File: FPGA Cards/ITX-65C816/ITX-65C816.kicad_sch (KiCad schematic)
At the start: 4 parts, among them J1 Conn_02x22_Odd_Even, U1 W65C816S6TQG-14

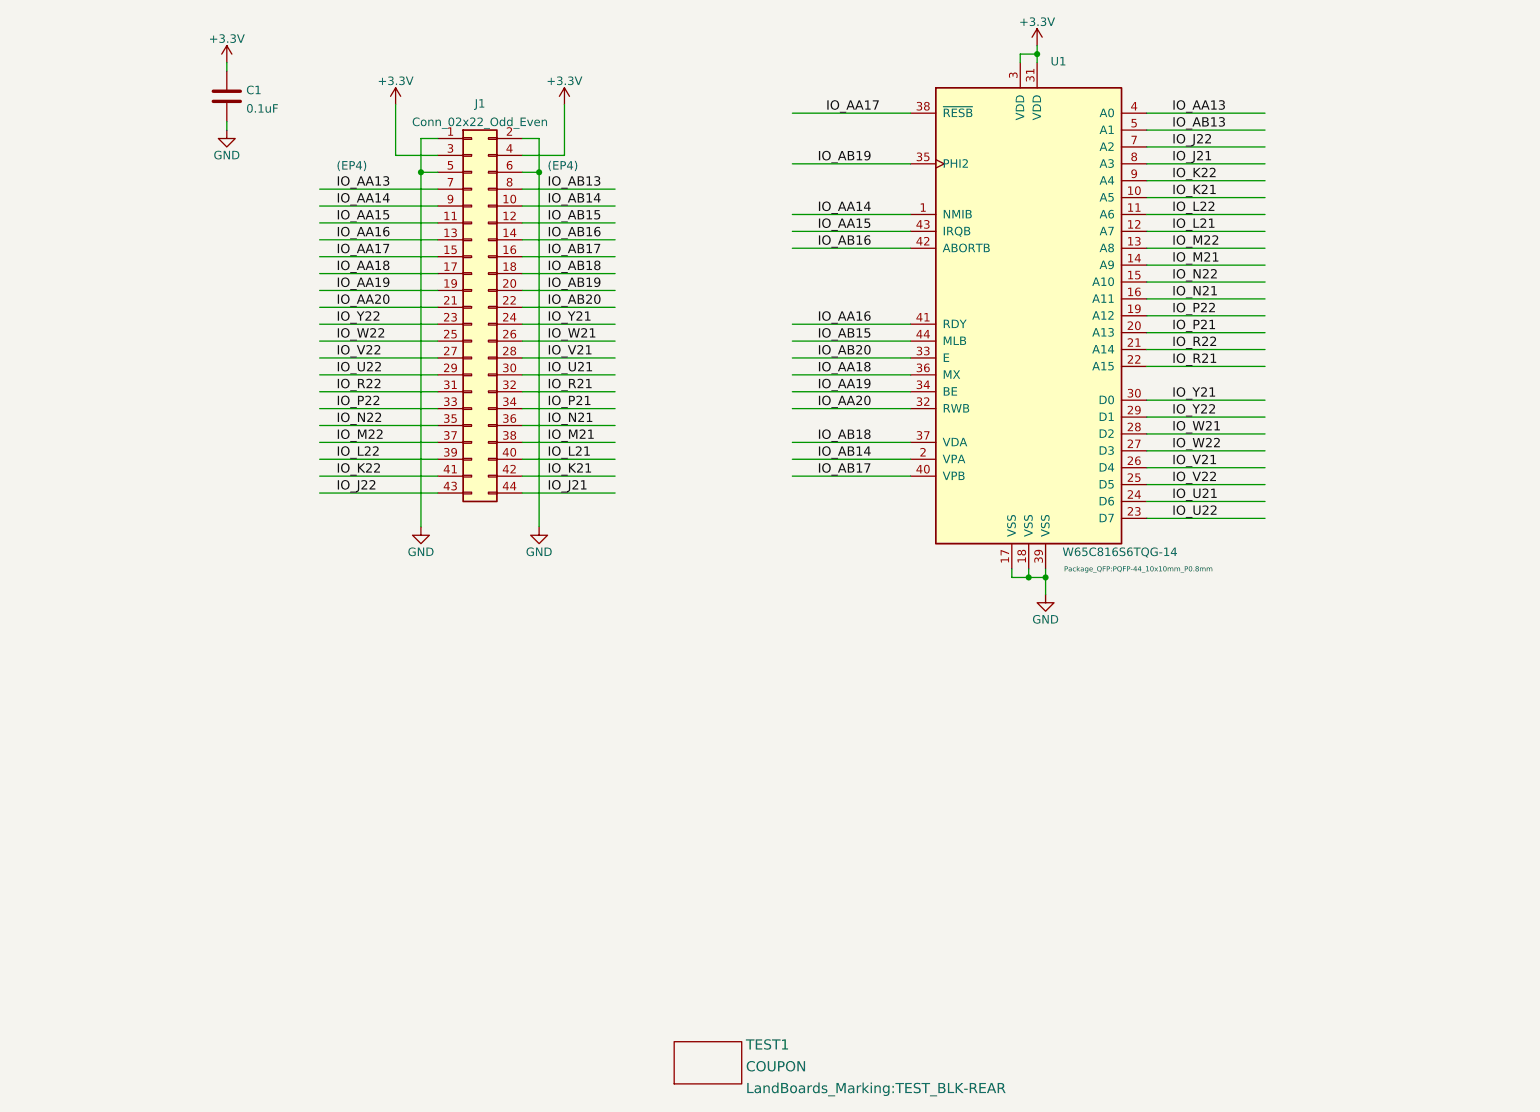
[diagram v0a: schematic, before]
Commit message: update ITX design files
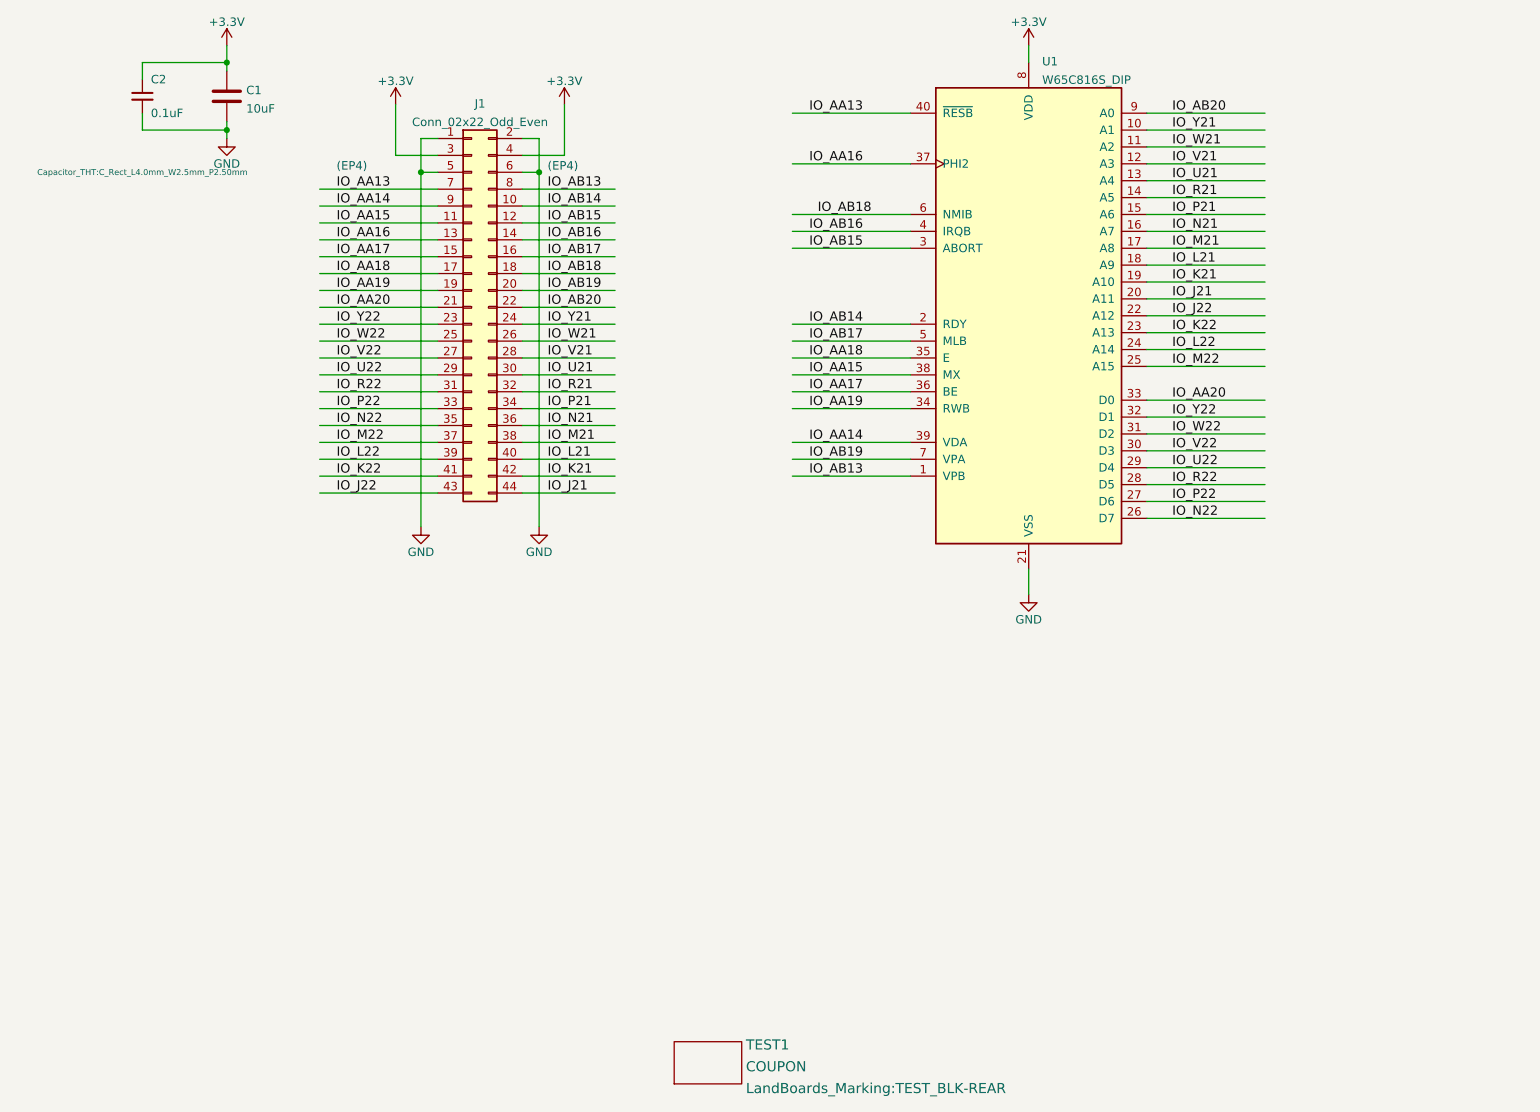
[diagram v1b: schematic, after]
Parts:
- removed U1: W65C816S6TQG-14, Package_QFP:PQFP-44_10x10mm_P0.8mm, symbol LandBoards_Semis:W65C816S
- added C2: 0.1uF, Capacitor_THT:C_Rect_L4.0mm_W2.5mm_P2.50mm, symbol Device:C_Small
- added U1: W65C816S_DIP, Package_DIP:DIP-40_W15.24mm_Socket, symbol LandBoards_Semis:W65C816S_DIP
- C1: value 0.1uF -> 10uF; footprint (none) -> Capacitor_THT:CP_Radial_D5.0mm_P2.50mm
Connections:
- net +3V3: now also C2.1, U1.8 (VDD)
- net GND: now also C2.2, U1.21 (VSS)
- net IO_AA13: now also U1.40 (~{RESB})
- net IO_AA14: now also U1.39 (VDA)
- net IO_AA15: now also U1.38 (MX)
- net IO_AA16: now also U1.37 (PHI2)
- net IO_AA17: now also U1.36 (BE)
- net IO_AA18: now also U1.35 (E)
- net IO_AA19: now also U1.34 (RWB)
- net IO_AA20: now also U1.33 (D0)
- net IO_AB13: now also U1.1 (VPB)
- net IO_AB14: now also U1.2 (RDY)
- net IO_AB15: now also U1.3 (ABORT)
- net IO_AB16: now also U1.4 (IRQB)
- net IO_AB17: now also U1.5 (MLB)
- net IO_AB18: now also U1.6 (NMIB)
- net IO_AB19: now also U1.7 (VPA)
- net IO_AB20: now also U1.9 (A0)
- net IO_J21: now also U1.20 (A11)
- net IO_J22: now also U1.22 (A12)
- net IO_K21: now also U1.19 (A10)
- net IO_K22: now also U1.23 (A13)
- net IO_L21: now also U1.18 (A9)
- net IO_L22: now also U1.24 (A14)
- net IO_M21: now also U1.17 (A8)
- net IO_M22: now also U1.25 (A15)
- net IO_N21: now also U1.16 (A7)
- net IO_N22: now also U1.26 (D7)
- net IO_P21: now also U1.15 (A6)
- net IO_P22: now also U1.27 (D6)
- net IO_R21: now also U1.14 (A5)
- net IO_R22: now also U1.28 (D5)
- net IO_U21: now also U1.13 (A4)
- net IO_U22: now also U1.29 (D4)
- net IO_V21: now also U1.12 (A3)
- net IO_V22: now also U1.30 (D3)
- net IO_W21: now also U1.11 (A2)
- net IO_W22: now also U1.31 (D2)
- net IO_Y21: now also U1.10 (A1)
- net IO_Y22: now also U1.32 (D1)

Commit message: ITX cards
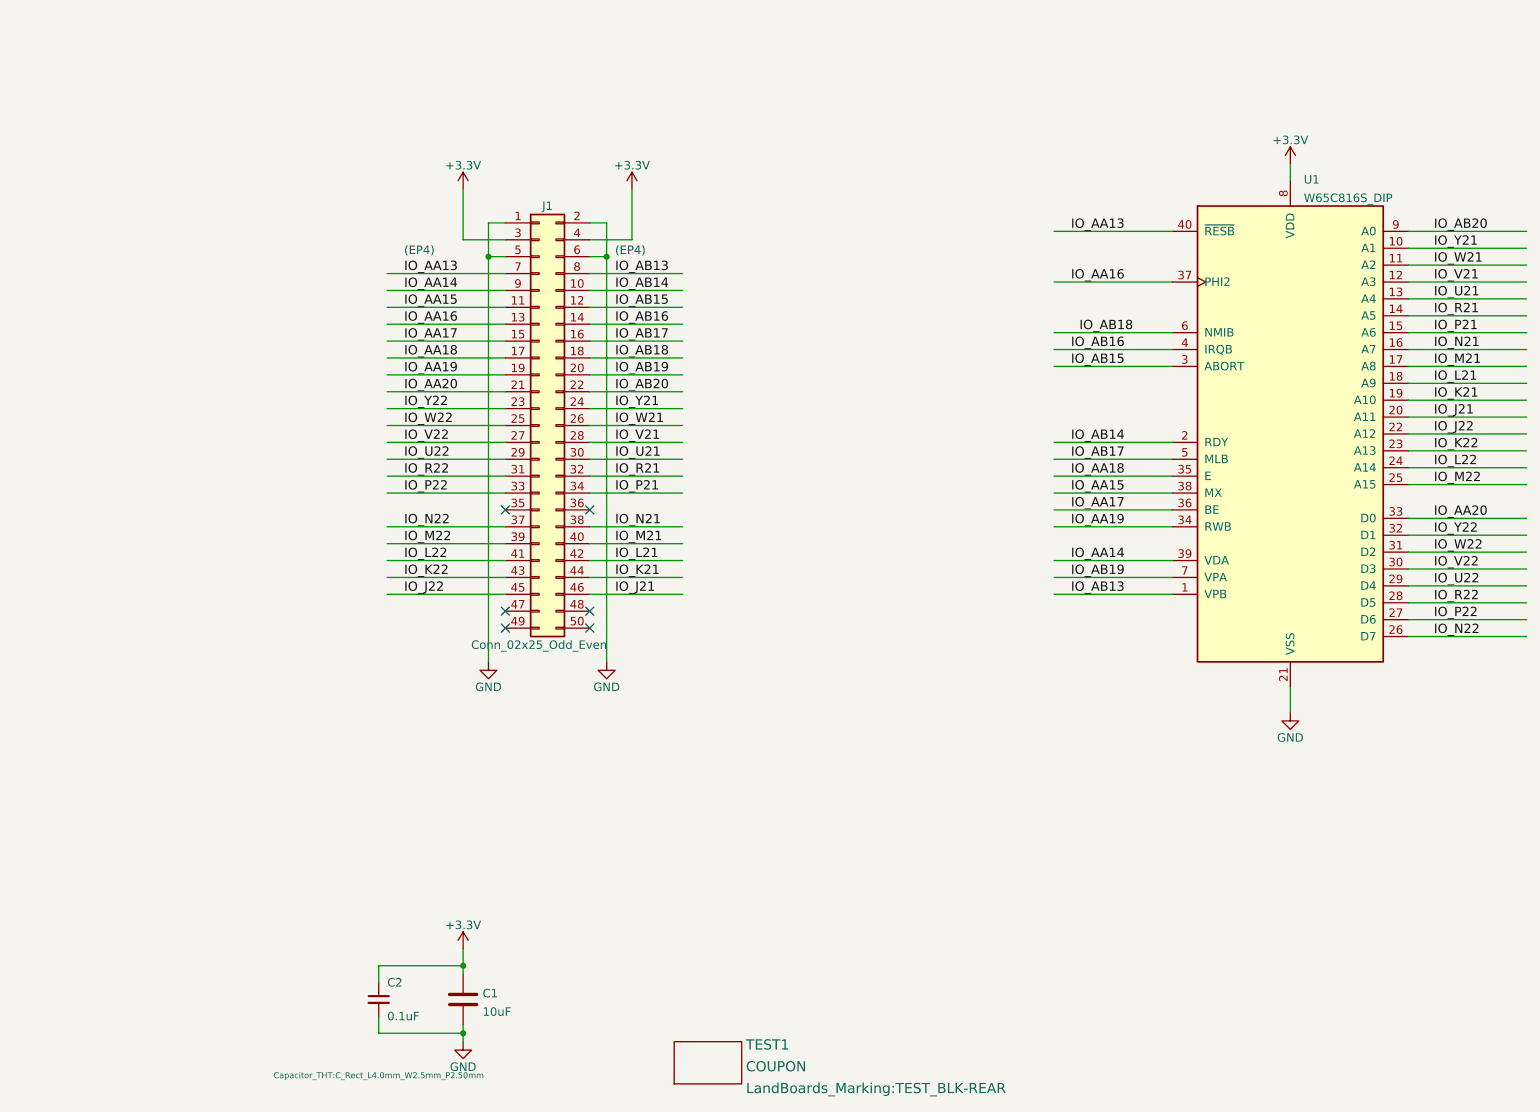
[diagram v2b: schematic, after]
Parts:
- removed J1: Conn_02x22_Odd_Even, Connector_PinHeader_2.54mm:PinHeader_2x22_P2.54mm_Horizontal, symbol Connector_Generic:Conn_02x22_Odd_Even
- added J1: Conn_02x25_Odd_Even, Connector_PinHeader_2.54mm:PinHeader_2x25_P2.54mm_Horizontal, symbol Connector_Generic:Conn_02x25_Odd_Even
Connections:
- net +3V3: now also J1.3 (Pin_3), J1.4 (Pin_4)
- net GND: now also J1.1 (Pin_1), J1.2 (Pin_2), J1.5 (Pin_5), J1.6 (Pin_6)
- net IO_AA13: now also J1.7 (Pin_7)
- net IO_AA14: now also J1.9 (Pin_9)
- net IO_AA15: now also J1.11 (Pin_11)
- net IO_AA16: now also J1.13 (Pin_13)
- net IO_AA17: now also J1.15 (Pin_15)
- net IO_AA18: now also J1.17 (Pin_17)
- net IO_AA19: now also J1.19 (Pin_19)
- net IO_AA20: now also J1.21 (Pin_21)
- net IO_AB13: now also J1.8 (Pin_8)
- net IO_AB14: now also J1.10 (Pin_10)
- net IO_AB15: now also J1.12 (Pin_12)
- net IO_AB16: now also J1.14 (Pin_14)
- net IO_AB17: now also J1.16 (Pin_16)
- net IO_AB18: now also J1.18 (Pin_18)
- net IO_AB19: now also J1.20 (Pin_20)
- net IO_AB20: now also J1.22 (Pin_22)
- net IO_J21: now also J1.46 (Pin_46)
- net IO_J22: now also J1.45 (Pin_45)
- net IO_K21: now also J1.44 (Pin_44)
- net IO_K22: now also J1.43 (Pin_43)
- net IO_L21: now also J1.42 (Pin_42)
- net IO_L22: now also J1.41 (Pin_41)
- net IO_M21: now also J1.40 (Pin_40)
- net IO_M22: now also J1.39 (Pin_39)
- net IO_N21: now also J1.38 (Pin_38)
- net IO_N22: now also J1.37 (Pin_37)
- net IO_P21: now also J1.34 (Pin_34)
- net IO_P22: now also J1.33 (Pin_33)
- net IO_R21: now also J1.32 (Pin_32)
- net IO_R22: now also J1.31 (Pin_31)
- net IO_U21: now also J1.30 (Pin_30)
- net IO_U22: now also J1.29 (Pin_29)
- net IO_V21: now also J1.28 (Pin_28)
- net IO_V22: now also J1.27 (Pin_27)
- net IO_W21: now also J1.26 (Pin_26)
- net IO_W22: now also J1.25 (Pin_25)
- net IO_Y21: now also J1.24 (Pin_24)
- net IO_Y22: now also J1.23 (Pin_23)
- no-connect marks 0 -> 6
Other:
- moved on the sheet: C1, C2, U1

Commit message: ITX card files - ordered
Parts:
- J1: footprint Connector_PinHeader_2.54mm:PinHeader_2x25_P2.54mm_Horizontal -> LandBoards_Conns:PinHeader_2x25_P2.54mm_Horizontal-FLIPPED
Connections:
- net IO_AA13: now also J1.8 (Pin_8); no longer J1.7 (Pin_7)
- net IO_AA14: now also J1.10 (Pin_10); no longer J1.9 (Pin_9)
- net IO_AA15: now also J1.12 (Pin_12); no longer J1.11 (Pin_11)
- net IO_AA16: now also J1.14 (Pin_14); no longer J1.13 (Pin_13)
- net IO_AA17: now also J1.16 (Pin_16); no longer J1.15 (Pin_15)
- net IO_AA18: now also J1.18 (Pin_18); no longer J1.17 (Pin_17)
- net IO_AA19: now also J1.20 (Pin_20); no longer J1.19 (Pin_19)
- net IO_AA20: now also J1.22 (Pin_22); no longer J1.21 (Pin_21)
- net IO_AB13: now also J1.7 (Pin_7); no longer J1.8 (Pin_8)
- net IO_AB14: now also J1.9 (Pin_9); no longer J1.10 (Pin_10)
- net IO_AB15: now also J1.11 (Pin_11); no longer J1.12 (Pin_12)
- net IO_AB16: now also J1.13 (Pin_13); no longer J1.14 (Pin_14)
- net IO_AB17: now also J1.15 (Pin_15); no longer J1.16 (Pin_16)
- net IO_AB18: now also J1.17 (Pin_17); no longer J1.18 (Pin_18)
- net IO_AB19: now also J1.19 (Pin_19); no longer J1.20 (Pin_20)
- net IO_AB20: now also J1.21 (Pin_21); no longer J1.22 (Pin_22)
- net IO_J21: now also J1.45 (Pin_45); no longer J1.46 (Pin_46)
- net IO_J22: now also J1.46 (Pin_46); no longer J1.45 (Pin_45)
- net IO_K21: now also J1.43 (Pin_43); no longer J1.44 (Pin_44)
- net IO_K22: now also J1.44 (Pin_44); no longer J1.43 (Pin_43)
- net IO_L21: now also J1.41 (Pin_41); no longer J1.42 (Pin_42)
- net IO_L22: now also J1.42 (Pin_42); no longer J1.41 (Pin_41)
- net IO_M21: now also J1.39 (Pin_39); no longer J1.40 (Pin_40)
- net IO_M22: now also J1.40 (Pin_40); no longer J1.39 (Pin_39)
- net IO_N21: now also J1.37 (Pin_37); no longer J1.38 (Pin_38)
- net IO_N22: now also J1.38 (Pin_38); no longer J1.37 (Pin_37)
- net IO_P21: now also J1.33 (Pin_33); no longer J1.34 (Pin_34)
- net IO_P22: now also J1.34 (Pin_34); no longer J1.33 (Pin_33)
- net IO_R21: now also J1.31 (Pin_31); no longer J1.32 (Pin_32)
- net IO_R22: now also J1.32 (Pin_32); no longer J1.31 (Pin_31)
- net IO_U21: now also J1.29 (Pin_29); no longer J1.30 (Pin_30)
- net IO_U22: now also J1.30 (Pin_30); no longer J1.29 (Pin_29)
- net IO_V21: now also J1.27 (Pin_27); no longer J1.28 (Pin_28)
- net IO_V22: now also J1.28 (Pin_28); no longer J1.27 (Pin_27)
- net IO_W21: now also J1.25 (Pin_25); no longer J1.26 (Pin_26)
- net IO_W22: now also J1.26 (Pin_26); no longer J1.25 (Pin_25)
- net IO_Y21: now also J1.23 (Pin_23); no longer J1.24 (Pin_24)
- net IO_Y22: now also J1.24 (Pin_24); no longer J1.23 (Pin_23)
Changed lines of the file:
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@@
     (pin "1")
   )
-  (symbol (lib_id "Connector_Generic:Conn_02x25_Odd_Even") (at 78.74 97.79 0) (unit 1)
+  (symbol (lib_id "Connector_Generic:Conn_02x25_Odd_Even") (at 81.28 97.79 0) (mirror y) (unit 1)
     (in_bom yes) (on_board yes)
     (property "Reference" "J1" (id 0) (at 80.01 64.77 0))
-    (property "Value" "Conn_02x25_Odd_Even" (id 1) (at 78.74 130.81 0))
-    (property "Footprint" "Connector_PinHeader_2.54mm:PinHeader_2x25_P2.54mm_Horizontal" (id 2) (at 78.74 97.79 0)
+    (property "Value" "Conn_02x25_Odd_Even" (id 1) (at 81.28 130.81 0))
+    (property "Footprint" "LandBoards_Conns:PinHeader_2x25_P2.54mm_Horizontal-FLIPPED" (id 2) (at 81.28 97.79 0)
       (effects (font (size 1.27 1.27)) hide)
     )
-    (property "Datasheet" "~" (id 3) (at 78.74 97.79 0)
+    (property "Datasheet" "~" (id 3) (at 81.28 97.79 0)
       (effects (font (size 1.27 1.27)) hide)
     )
@@
       (reference "C2") (unit 1) (value "0.1uF") (footprint "Capacitor_THT:C_Rect_L4.0mm_W2.5mm_P2.50mm")
     )
-    (path "/b9349937-f4be-4789-b58b-595f2ab9279b"
-      (reference "J1") (unit 1) (value "Conn_02x25_Odd_Even") (footprint "Connector_PinHeader_2.54mm:PinHeader_2x25_P2.54mm_Horizontal")
+    (path "/ca12753c-a5f4-49a4-bb14-a01420a86edb"
+      (reference "J1") (unit 1) (value "Conn_02x25_Odd_Even") (footprint "LandBoards_Conns:PinHeader_2x25_P2.54mm_Horizontal-FLIPPED")
     )
     (path "/215b26cf-6f97-4309-90bf-dbb0f7eb82b9"
